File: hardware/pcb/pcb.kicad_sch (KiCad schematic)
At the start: 5 parts, among them J1 PRT-12639, K1 KEYSW, U1 RP2040_Zero, U2 Nice_Nano_V2

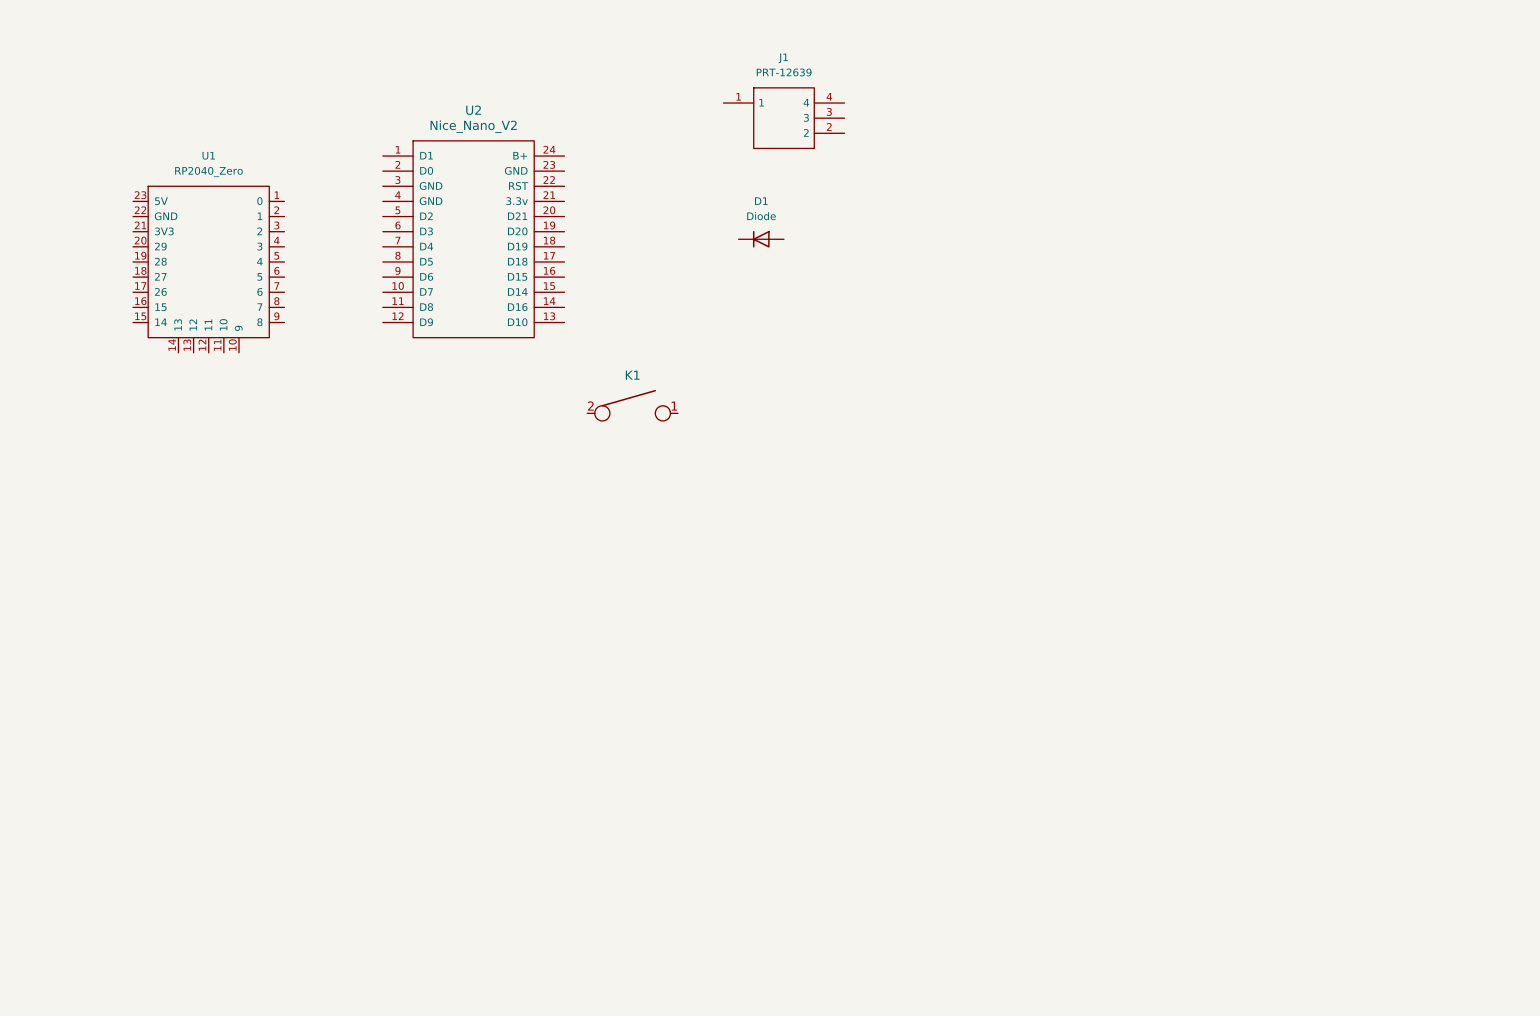
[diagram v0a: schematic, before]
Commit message: added 6X8 matrix and global labels
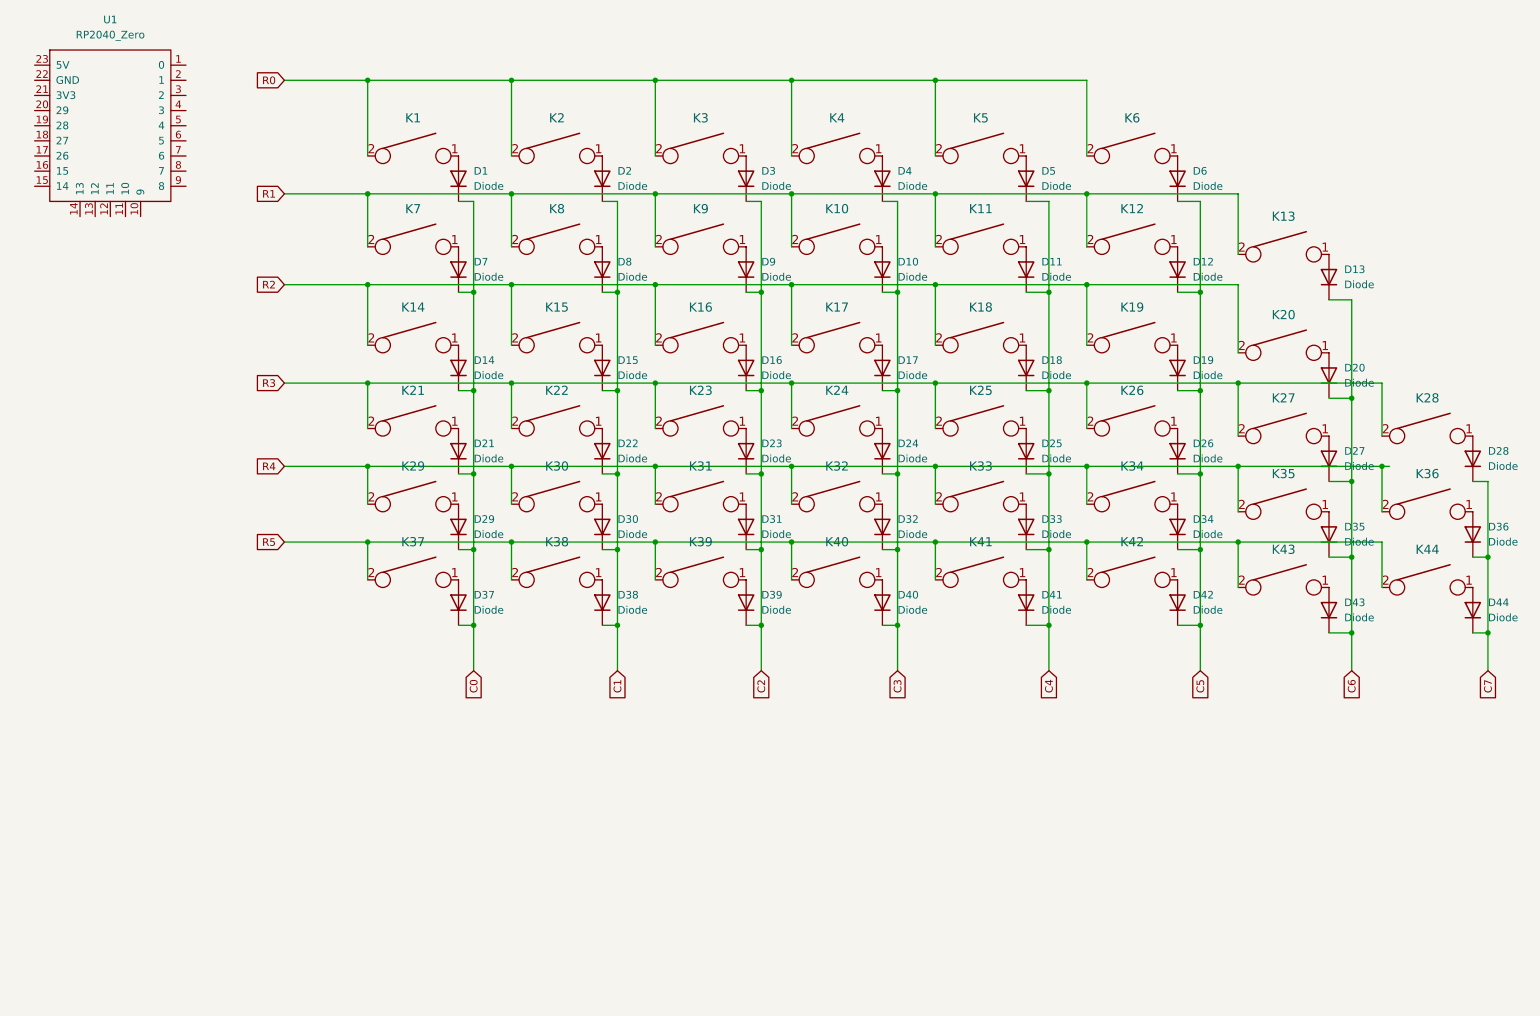
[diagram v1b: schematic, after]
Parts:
- removed J1: PRT-12639, PRT12639, symbol PRT-12639:PRT-12639
- removed U2: Nice_Nano_V2, ScottoKeebs_MCU:Nice_Nano_V2, symbol ScottoKeebs:MCU_Nice_Nano_V2
- added D10, D11, D12, D13, D14, D15, D16, D17, D18, D19, D2, D20, D21, D22, D23, D24, D25, D26, D27, D28, D29, D3, D30, D31, D32, D33, D34, D35, D36, D37, D38, D39, D4, D40, D41, D42, D43, D44, D5, D6, D7, D8, D9: Diode, ScottoKeebs_Components:Diode_DO-35, symbol ScottoKeebs:Placeholder_Diode
- added K10, K11, K12, K13, K14, K15, K16, K17, K18, K19, K2, K20, K21, K22, K23, K24, K25, K26, K27, K28, K29, K3, K30, K31, K32, K33, K34, K35, K36, K37, K38, K39, K4, K40, K41, K42, K43, K44, K5, K6, K7, K8, K9: KEYSW, vbdox:Kailh_MX_Socket_reversible, symbol Kailh_socket_MX_reversible:KEYSW
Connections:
- net at K1.1: now also D1.2 (A)
- net R0: now reaches K1.2
- net R0: now also K2.2, K3.2, K4.2, K5.2, K6.2
- net C0: now reaches D1.1 (K)
- net C0: now also D14.1 (K), D21.1 (K), D29.1 (K), D37.1 (K), D7.1 (K)
- new net: D2.2 (A), K2.1
- new net: D5.2 (A), K5.1
- new net: D31.2 (A), K31.1
- new net: D21.2 (A), K21.1
- new net: D32.2 (A), K32.1
- new net: D40.2 (A), K40.1
- new net: D9.2 (A), K9.1
- new net: D10.2 (A), K10.1
- new net: D11.2 (A), K11.1
- new net: D24.2 (A), K24.1
- new net: D33.2 (A), K33.1
- new net: D38.2 (A), K38.1
- new net: D25.2 (A), K25.1
- new net: D20.2 (A), K20.1
- new net: D7.2 (A), K7.1
- new net: D4.2 (A), K4.1
- new net: D17.2 (A), K17.1
- new net: D6.2 (A), K6.1
- new net: D36.2 (A), K36.1
- new net: D37.2 (A), K37.1
- new net: D18.2 (A), K18.1
- new net: D30.2 (A), K30.1
- new net: D8.2 (A), K8.1
- new net: D39.2 (A), K39.1
- new net: D3.2 (A), K3.1
- new net: D28.2 (A), K28.1
- new net: D22.2 (A), K22.1
- new net: D42.2 (A), K42.1
- new net: D35.2 (A), K35.1
- new net: D14.2 (A), K14.1
- new net: D23.2 (A), K23.1
- new net: D43.2 (A), K43.1
- new net: D27.2 (A), K27.1
- new net: D12.2 (A), K12.1
- new net: D16.2 (A), K16.1
- new net: D34.2 (A), K34.1
- new net: D44.2 (A), K44.1
- new net: D15.2 (A), K15.1
- new net: D41.2 (A), K41.1
- new net: D29.2 (A), K29.1
- new net: D26.2 (A), K26.1
- new net: D13.2 (A), K13.1
- new net: D19.2 (A), K19.1
- new net C1: D15.1 (K), D2.1 (K), D22.1 (K), D30.1 (K), D38.1 (K), D8.1 (K)
- new net C2: D16.1 (K), D23.1 (K), D3.1 (K), D31.1 (K), D39.1 (K), D9.1 (K)
- new net C3: D10.1 (K), D17.1 (K), D24.1 (K), D32.1 (K), D4.1 (K), D40.1 (K)
- new net C4: D11.1 (K), D18.1 (K), D25.1 (K), D33.1 (K), D41.1 (K), D5.1 (K)
- new net C5: D12.1 (K), D19.1 (K), D26.1 (K), D34.1 (K), D42.1 (K), D6.1 (K)
- new net C6: D13.1 (K), D20.1 (K), D27.1 (K), D35.1 (K), D43.1 (K)
- new net C7: D28.1 (K), D36.1 (K), D44.1 (K)
- new net R1: K10.2, K11.2, K12.2, K13.2, K7.2, K8.2, K9.2
- new net R2: K14.2, K15.2, K16.2, K17.2, K18.2, K19.2, K20.2
- new net R3: K21.2, K22.2, K23.2, K24.2, K25.2, K26.2, K27.2, K28.2
- new net R4: K29.2, K30.2, K31.2, K32.2, K33.2, K34.2, K35.2, K36.2
- new net R5: K37.2, K38.2, K39.2, K40.2, K41.2, K42.2, K43.2, K44.2
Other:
- company: (none) -> VB inc.
- title: (none) -> vbdox
- moved on the sheet: U1

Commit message: schema init
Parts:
- added J2: PRT-12639, vbdox:PRT12639, symbol PRT-12639:PRT-12639
- added R1, R2: 2.2K, ScottoKeebs_Components:Diode_DO-35, symbol Device:R
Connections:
- net C0: now also U1.1 (0)
- net C1: now also U1.2 (1)
- net C2: now also U1.3 (2)
- net C3: now also U1.4 (3)
- net C4: now also U1.5 (4)
- net C5: now also U1.6 (5)
- net C6: now also U1.7 (6)
- net C7: now also U1.8 (7)
- net R0: now also U1.20 (29)
- net R1: now also U1.19 (28)
- net R2: now also U1.18 (27)
- net R3: now also U1.17 (26)
- net R4: now also U1.16 (15)
- net R5: now also U1.15 (14)
- net SDA: now reaches U1.13 (12)
- net SDA: now also J2.2, R2.1
- net SCL: now reaches U1.14 (13)
- net SCL: now also J2.3, R1.1
- net GND: now reaches U1.22 (GND)
- net GND: now also J2.1
- net VCC: now reaches U1.23 (5V)
- net VCC: now also J2.4, R1.2, R2.2
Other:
- moved on the sheet: D1, D10, D11, D12, D13, D14, D15, D16, D17, D18, D19, D2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
